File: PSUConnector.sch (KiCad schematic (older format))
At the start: 1 part

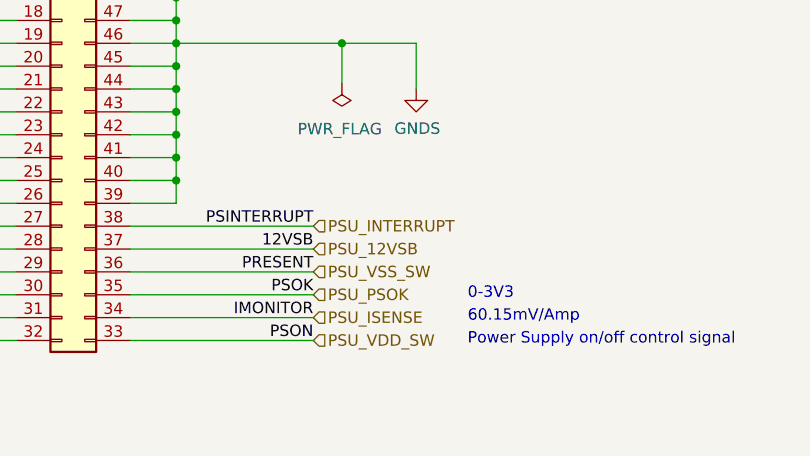
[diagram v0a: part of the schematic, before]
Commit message: UPDATED SWITCH WIRING
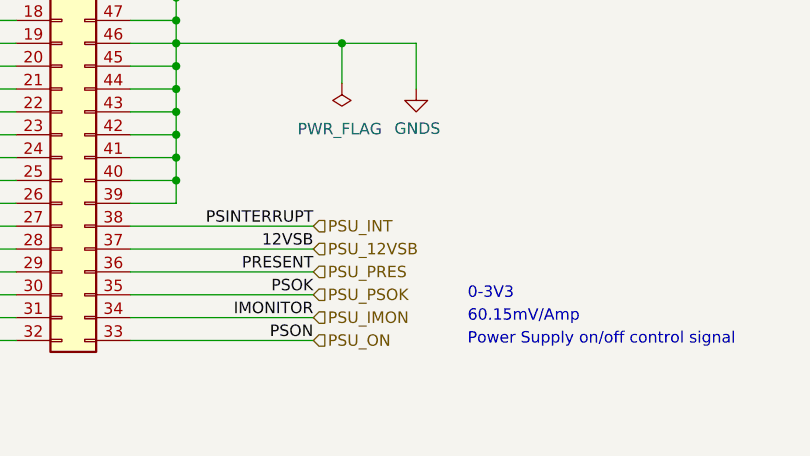
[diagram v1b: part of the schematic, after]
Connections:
- net PSU_INTERRUPT renamed PSU_INT
- net PSU_ISENSE renamed PSU_IMON
- net PSU_VDD_SW renamed PSU_ON
- net PSU_VSS_SW renamed PSU_PRES
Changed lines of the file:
@@
 PSU_12VSB
 Text HLabel 5200 5350 2    50   Input ~ 0
-PSU_VDD_SW
+PSU_ON
 Text HLabel 5200 5050 2    50   Input ~ 0
-PSU_VSS_SW
+PSU_PRES
 Text HLabel 5200 5150 2    50   Input ~ 0
 PSU_PSOK
@@
 	4400 5250 5200 5250
 Text HLabel 5200 5250 2    50   Input ~ 0
-PSU_ISENSE
+PSU_IMON
 Text Notes 5875 5175 0    50   ~ 0
 0-3V3
@@
 	4400 4850 5200 4850
 Text HLabel 5200 4850 2    50   Input ~ 0
-PSU_INTERRUPT
+PSU_INT
 Text Label 5200 4850 2    50   ~ 0
 PSINTERRUPT

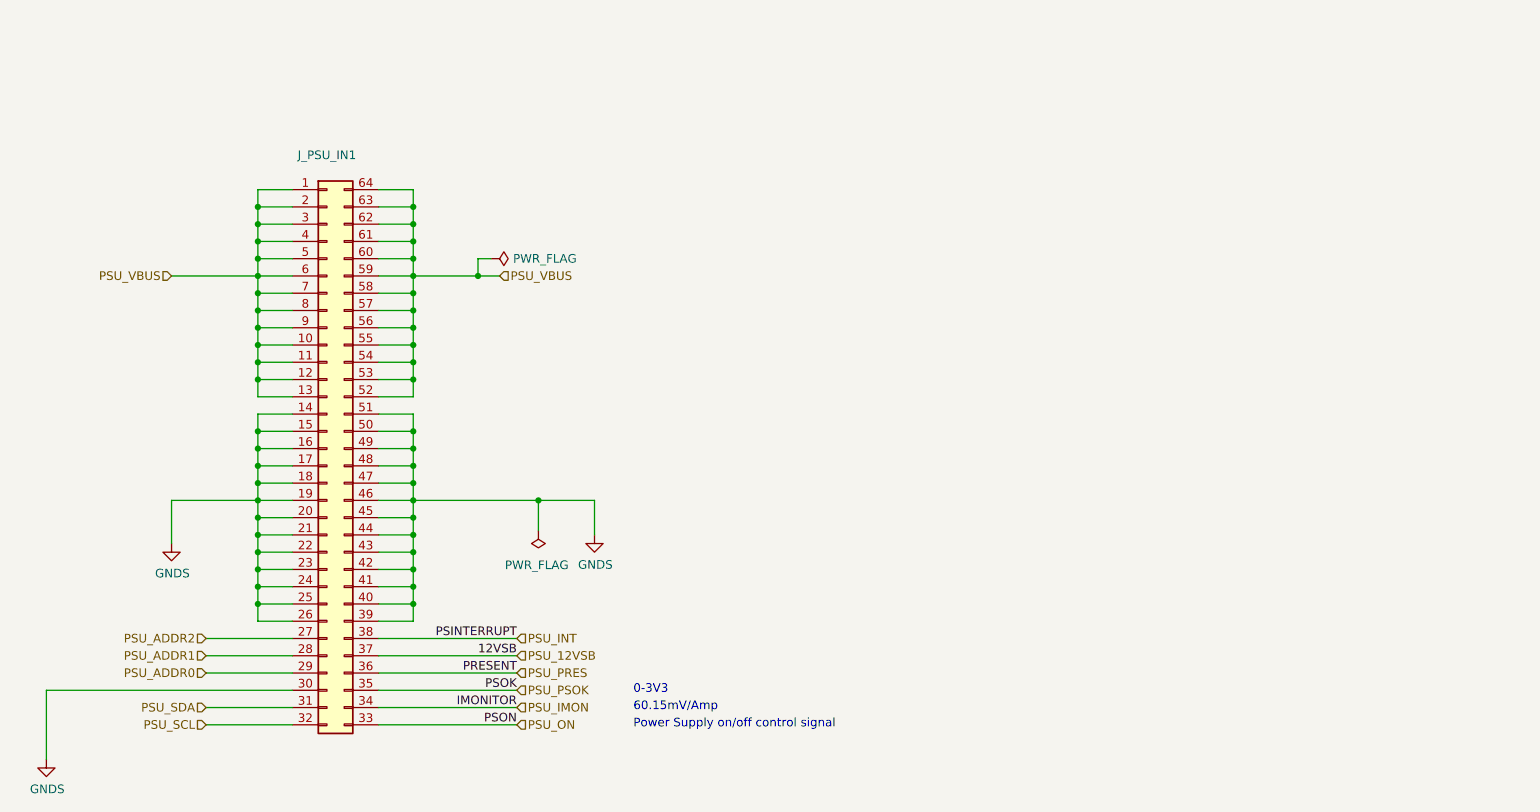
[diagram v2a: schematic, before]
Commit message: updated hw
- added SMBUS address HW 
- Changed Isolated DC Module to TI SimpleSwitcher IC
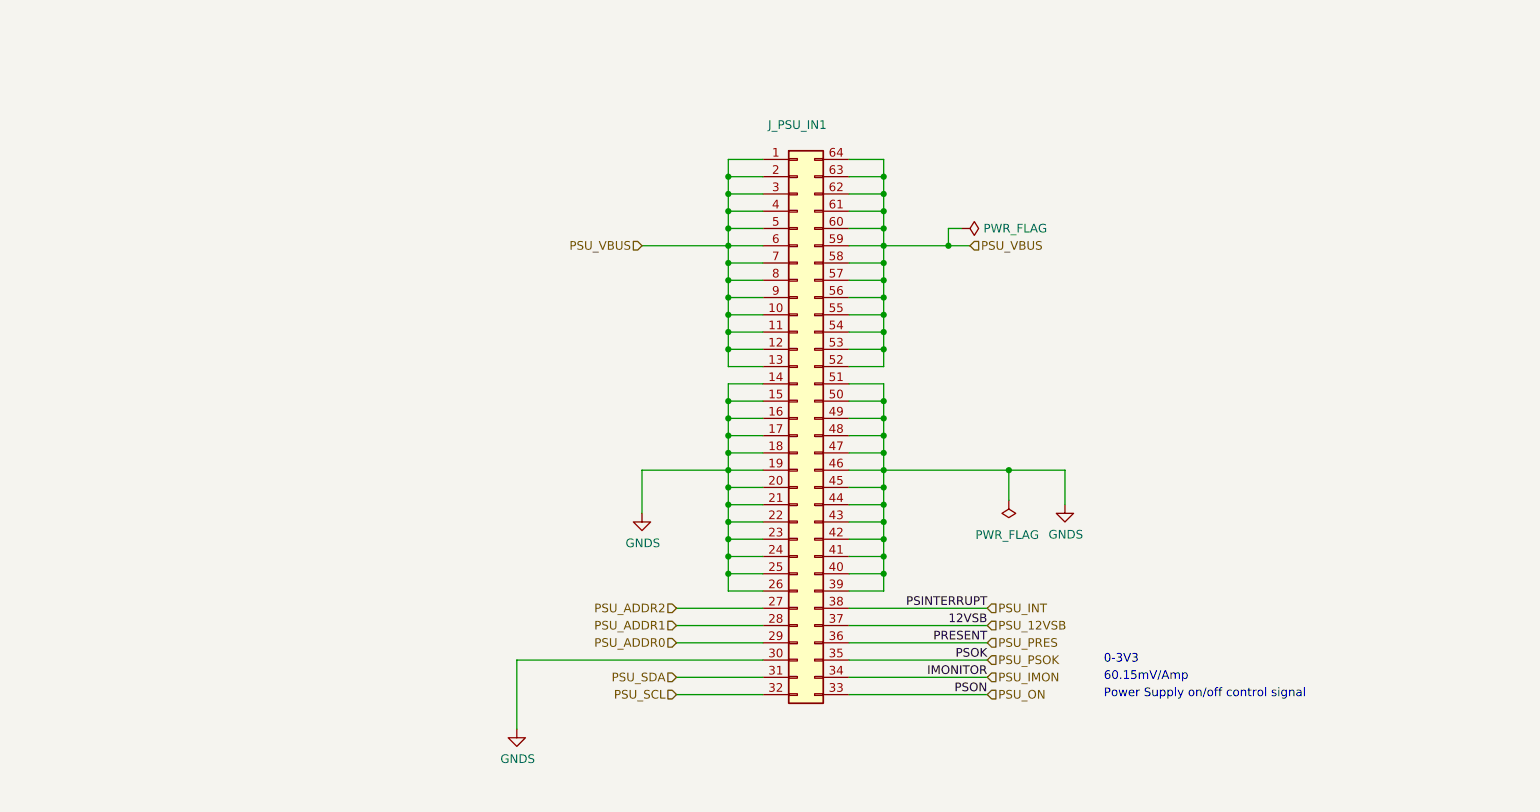
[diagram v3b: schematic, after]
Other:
- moved on the sheet: J_PSU_IN1

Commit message: Completed RevA
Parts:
- added TP11, TP12, TP13, TP14, TP15, TP16, TP17, TP18, TP19, TP20, TP21, TP3, TP4: TestPoint, TestPoint:TestPoint_Pad_1.0x1.0mm, symbol Connector:TestPoint
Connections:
- net GNDS: now also TP16.1, TP3.1
- net PSU_12VSB: now also TP4.1
- net PSU_ADDR0: now also TP13.1
- net PSU_ADDR1: now also TP12.1
- net PSU_ADDR2: now also TP11.1
- net PSU_IMON: now also TP19.1
- net PSU_INT: now also TP17.1
- net PSU_ON: now also TP18.1
- net PSU_PRES: now also TP21.1
- net PSU_PSOK: now also TP20.1
- net PSU_SCL: now also TP15.1
- net PSU_SDA: now also TP14.1
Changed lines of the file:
@@
 Text HLabel 6125 4675 0    50   Input ~ 0
 PSU_ADDR2
+$Comp
+L Connector:TestPoint TP?
+U 1 1 5F18B86B
+P 8925 3025
+AR Path="/5F02F4E9/5F18B86B" Ref="TP?"  Part="1"
+AR Path="/5EFF0F4B/5F18B86B" Ref="TP3"  Part="1"
+F 0 "TP3" H 8983 3143 50  0000 L CNN
+F 1 "TestPoint" H 8983 3052 50  0000 L CNN
+F 2 "TestPoint:TestPoint_Pad_1.0x1.0mm" H 9125 3025 50  0001 C CNN
+F 3 "~" H 9125 3025 50  0001 C CNN
+	1    8925 3025
+	1    0    0    -1
+$EndComp
+$Comp
+L Connector:TestPoint TP?
+U 1 1 5F18F46B
+P 9475 3025
+AR Path="/5F02F4E9/5F18F46B" Ref="TP?"  Part="1"
+AR Path="/5EFF0F4B/5F18F46B" Ref="TP4"  Part="1"
+F 0 "TP4" H 9533 3143 50  0000 L CNN
+F 1 "TestPoint" H 9533 3052 50  0000 L CNN
+F 2 "TestPoint:TestPoint_Pad_1.0x1.0mm" H 9675 3025 50  0001 C CNN
+F 3 "~" H 9675 3025 50  0001 C CNN
+	1    9475 3025
+	1    0    0    -1
+$EndComp
+Wire Wire Line
+	8925 3025 8925 3250
+$Comp
+L power:GNDS #PWR015
+U 1 1 5F196630
+P 8925 3250
+F 0 "#PWR015" H 8925 3000 50  0001 C CNN
+F 1 "GNDS" H 8930 3077 50  0000 C CNN
+F 2 "" H 8925 3250 50  0001 C CNN
+F 3 "" H 8925 3250 50  0001 C CNN
+	1    8925 3250
+	1    0    0    -1
+$EndComp
+Wire Wire Line
+	9475 3025 9475 3275
+Text HLabel 9475 3275 3    50   Input ~ 0
+PSU_12VSB
+$Comp
+L Connector:TestPoint TP?
+U 1 1 5F1D2F4B
+P 2925 2350
+AR Path="/5F02F4E9/5F1D2F4B" Ref="TP?"  Part="1"
+AR Path="/5EFF0F4B/5F1D2F4B" Ref="TP12"  Part="1"
+F 0 "TP12" H 2983 2468 50  0000 L CNN
+F 1 "TestPoint" H 2983 2377 50  0000 L CNN
+F 2 "TestPoint:TestPoint_Pad_1.0x1.0mm" H 3125 2350 50  0001 C CNN
+F 3 "~" H 3125 2350 50  0001 C CNN
+	1    2925 2350
+	1    0    0    -1
+$EndComp
+Wire Wire Line
+	2925 2350 2925 2575
+$Comp
+L Connector:TestPoint TP?
+U 1 1 5F1D6AD4
+P 3450 2350
+AR Path="/5F02F4E9/5F1D6AD4" Ref="TP?"  Part="1"
+AR Path="/5EFF0F4B/5F1D6AD4" Ref="TP13"  Part="1"
+F 0 "TP13" H 3508 2468 50  0000 L CNN
+F 1 "TestPoint" H 3508 2377 50  0000 L CNN
+F 2 "TestPoint:TestPoint_Pad_1.0x1.0mm" H 3650 2350 50  0001 C CNN
+F 3 "~" H 3650 2350 50  0001 C CNN
+	1    3450 2350
+	1    0    0    -1
+$EndComp
+Wire Wire Line
+	3450 2350 3450 2575
+$Comp
+L Connector:TestPoint TP?
+U 1 1 5F1DA7F0
+P 2425 2350
+AR Path="/5F02F4E9/5F1DA7F0" Ref="TP?"  Part="1"
+AR Path="/5EFF0F4B/5F1DA7F0" Ref="TP11"  Part="1"
+F 0 "TP11" H 2483 2468 50  0000 L CNN
+F 1 "TestPoint" H 2483 2377 50  0000 L CNN
+F 2 "TestPoint:TestPoint_Pad_1.0x1.0mm" H 2625 2350 50  0001 C CNN
+F 3 "~" H 2625 2350 50  0001 C CNN
+	1    2425 2350
+	1    0    0    -1
+$EndComp
+Wire Wire Line
+	2425 2350 2425 2575
+Text HLabel 3450 2575 3    50   Input ~ 0
+PSU_ADDR0
+Text HLabel 2925 2575 3    50   Input ~ 0
+PSU_ADDR1
+Text HLabel 2425 2575 3    50   Input ~ 0
+PSU_ADDR2
+$Comp
+L Connector:TestPoint TP?
+U 1 1 5F1FA07F
+P 2900 3825
+AR Path="/5F02F4E9/5F1FA07F" Ref="TP?"  Part="1"
+AR Path="/5EFF0F4B/5F1FA07F" Ref="TP15"  Part="1"
+F 0 "TP15" H 2958 3943 50  0000 L CNN
+F 1 "TestPoint" H 2958 3852 50  0000 L CNN
+F 2 "TestPoint:TestPoint_Pad_1.0x1.0mm" H 3100 3825 50  0001 C CNN
+F 3 "~" H 3100 3825 50  0001 C CNN
+	1    2900 3825
+	1    0    0    -1
+$EndComp
+Wire Wire Line
+	2900 3825 2900 4050
+$Comp
+L Connector:TestPoint TP?
+U 1 1 5F1FA086
+P 2400 3825
+AR Path="/5F02F4E9/5F1FA086" Ref="TP?"  Part="1"
+AR Path="/5EFF0F4B/5F1FA086" Ref="TP14"  Part="1"
+F 0 "TP14" H 2458 3943 50  0000 L CNN
+F 1 "TestPoint" H 2458 3852 50  0000 L CNN
+F 2 "TestPoint:TestPoint_Pad_1.0x1.0mm" H 2600 3825 50  0001 C CNN
+F 3 "~" H 2600 3825 50  0001 C CNN
+	1    2400 3825
+	1    0    0    -1
+$EndComp
+Wire Wire Line
+	2400 3825 2400 4050
+Text HLabel 2400 4050 3    50   Input ~ 0
+PSU_SDA
+Text HLabel 2900 4050 3    50   Input ~ 0
+PSU_SCL
+$Comp
+L Connector:TestPoint TP?
+U 1 1 5F208833
+P 2400 4925
+AR Path="/5F02F4E9/5F208833" Ref="TP?"  Part="1"
+AR Path="/5EFF0F4B/5F208833" Ref="TP16"  Part="1"
+F 0 "TP16" H 2458 5043 50  0000 L CNN
+F 1 "TestPoint" H 2458 4952 50  0000 L CNN
+F 2 "TestPoint:TestPoint_Pad_1.0x1.0mm" H 2600 4925 50  0001 C CNN
+F 3 "~" H 2600 4925 50  0001 C CNN
+	1    2400 4925
+	1    0    0    -1
+$EndComp
+Wire Wire Line
+	2400 4925 2400 5150
+$Comp
+L power:GNDS #PWR016
+U 1 1 5F20C83E
+P 2400 5150
+F 0 "#PWR016" H 2400 4900 50  0001 C CNN
+F 1 "GNDS" H 2405 4977 50  0000 C CNN
+F 2 "" H 2400 5150 50  0001 C CNN
+F 3 "" H 2400 5150 50  0001 C CNN
+	1    2400 5150
+	1    0    0    -1
+$EndComp
+$Comp
+L Connector:TestPoint TP?
+U 1 1 5F221423
+P 8975 1425
+AR Path="/5F02F4E9/5F221423" Ref="TP?"  Part="1"
+AR Path="/5EFF0F4B/5F221423" Ref="TP18"  Part="1"
+F 0 "TP18" H 9033 1543 50  0000 L CNN
+F 1 "TestPoint" H 9033 1452 50  0000 L CNN
+F 2 "TestPoint:TestPoint_Pad_1.0x1.0mm" H 9175 1425 50  0001 C CNN
+F 3 "~" H 9175 1425 50  0001 C CNN
+	1    8975 1425
+	1    0    0    -1
+$EndComp
+Wire Wire Line
+	8975 1425 8975 1650
+$Comp
+L Connector:TestPoint TP?
+U 1 1 5F225748
+P 9500 1425
+AR Path="/5F02F4E9/5F225748" Ref="TP?"  Part="1"
+AR Path="/5EFF0F4B/5F225748" Ref="TP19"  Part="1"
+F 0 "TP19" H 9558 1543 50  0000 L CNN
+F 1 "TestPoint" H 9558 1452 50  0000 L CNN
+F 2 "TestPoint:TestPoint_Pad_1.0x1.0mm" H 9700 1425 50  0001 C CNN
+F 3 "~" H 9700 1425 50  0001 C CNN
+	1    9500 1425
+	1    0    0    -1
+$EndComp
+Wire Wire Line
+	9500 1425 9500 1650
+Text HLabel 9500 1650 3    50   Input ~ 0
+PSU_IMON
+Text HLabel 8975 1650 3    50   Input ~ 0
+PSU_ON
+$Comp
+L Connector:TestPoint TP?
+U 1 1 5F24027B
+P 10075 1400
+AR Path="/5F02F4E9/5F24027B" Ref="TP?"  Part="1"
+AR Path="/5EFF0F4B/5F24027B" Ref="TP20"  Part="1"
+F 0 "TP20" H 10133 1518 50  0000 L CNN
+F 1 "TestPoint" H 10133 1427 50  0000 L CNN
+F 2 "TestPoint:TestPoint_Pad_1.0x1.0mm" H 10275 1400 50  0001 C CNN
+F 3 "~" H 10275 1400 50  0001 C CNN
+	1    10075 1400
+	1    0    0    -1
+$EndComp
+Wire Wire Line
+	10075 1400 10075 1650
+Text HLabel 10075 1650 3    50   Input ~ 0
+PSU_PSOK
+$Comp
+L Connector:TestPoint TP?
+U 1 1 5F257476
+P 8375 1425
+AR Path="/5F02F4E9/5F257476" Ref="TP?"  Part="1"
+AR Path="/5EFF0F4B/5F257476" Ref="TP17"  Part="1"
+F 0 "TP17" H 8433 1543 50  0000 L CNN
+F 1 "TestPoint" H 8433 1452 50  0000 L CNN
+F 2 "TestPoint:TestPoint_Pad_1.0x1.0mm" H 8575 1425 50  0001 C CNN
+F 3 "~" H 8575 1425 50  0001 C CNN
+	1    8375 1425
+	1    0    0    -1
+$EndComp
+Wire Wire Line
+	8375 1425 8375 1650
+Text HLabel 8375 1650 3    50   Input ~ 0
+PSU_INT
+Text HLabel 10550 1650 3    50   Input ~ 0
+PSU_PRES
+$Comp
+L Connector:TestPoint TP?
+U 1 1 5F263862
+P 10550 1425
+AR Path="/5F02F4E9/5F263862" Ref="TP?"  Part="1"
+AR Path="/5EFF0F4B/5F263862" Ref="TP21"  Part="1"
+F 0 "TP21" H 10608 1543 50  0000 L CNN
+F 1 "TestPoint" H 10608 1452 50  0000 L CNN
+F 2 "TestPoint:TestPoint_Pad_1.0x1.0mm" H 10750 1425 50  0001 C CNN
+F 3 "~" H 10750 1425 50  0001 C CNN
+	1    10550 1425
+	1    0    0    -1
+$EndComp
+Wire Wire Line
+	10550 1425 10550 1650
 $EndSCHEMATC
